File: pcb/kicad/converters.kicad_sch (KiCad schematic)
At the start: 48 parts, among them J2 NMJ4HCD2, U601 REF3033, U602 DAC7563SDGSR, U603 MCP6001-OT, U604 ADC141S626, U605 MCP6001-OT, U606 MCP6001-OT

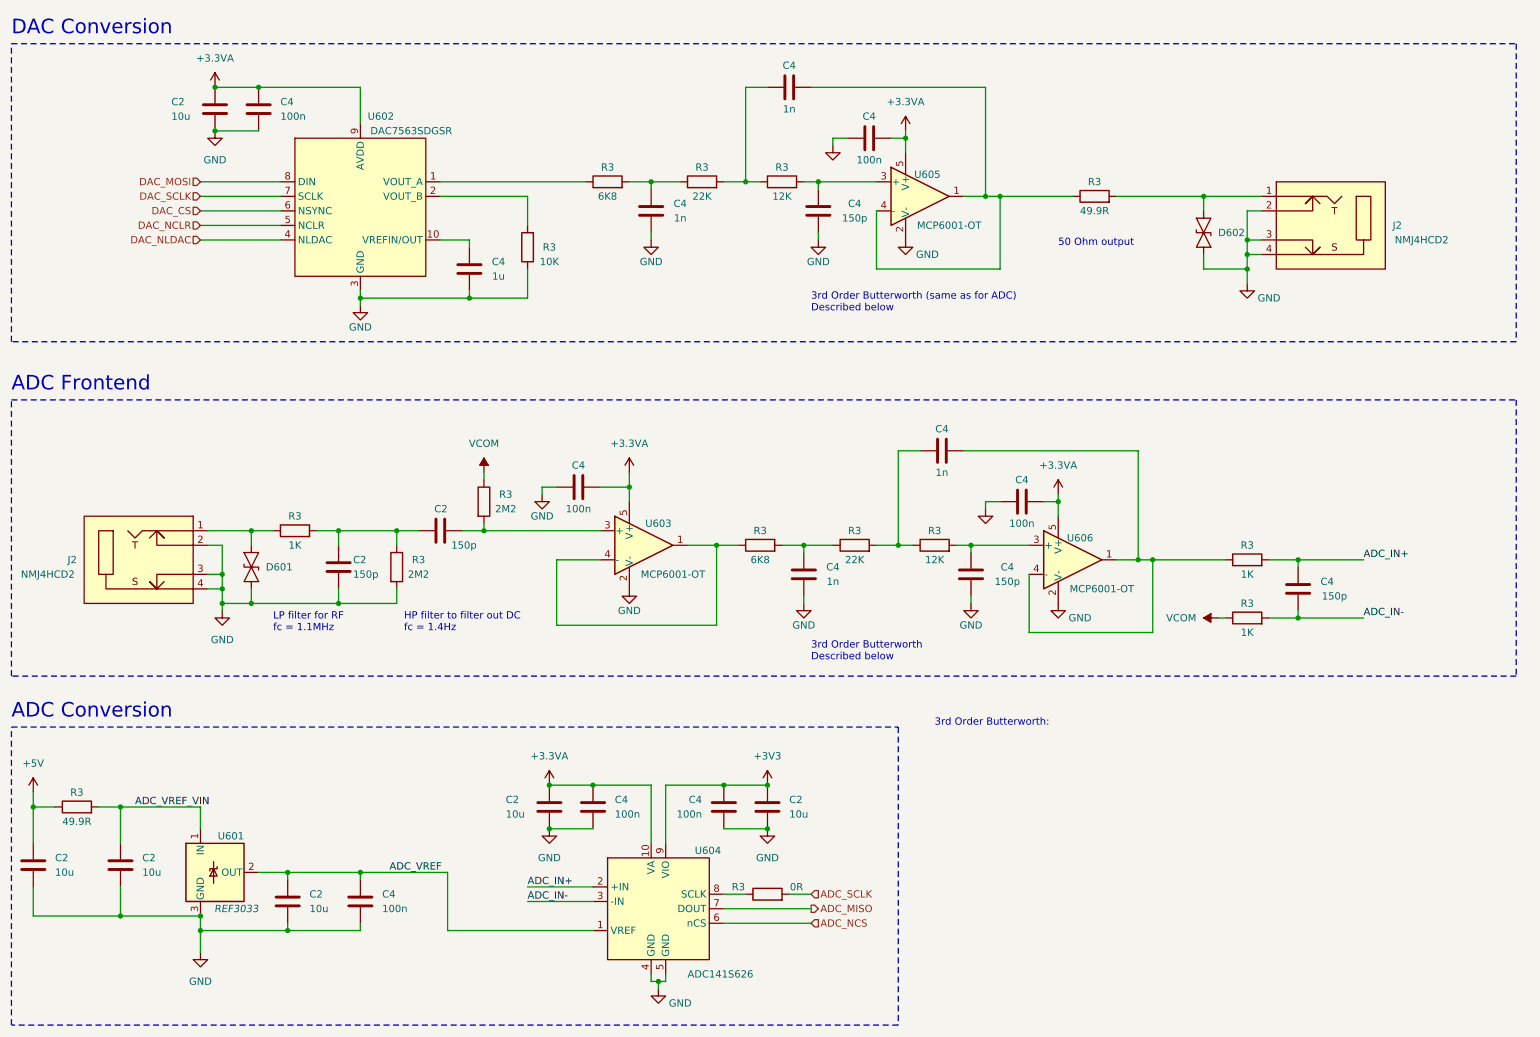
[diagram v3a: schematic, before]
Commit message: Add ltspice simulations.
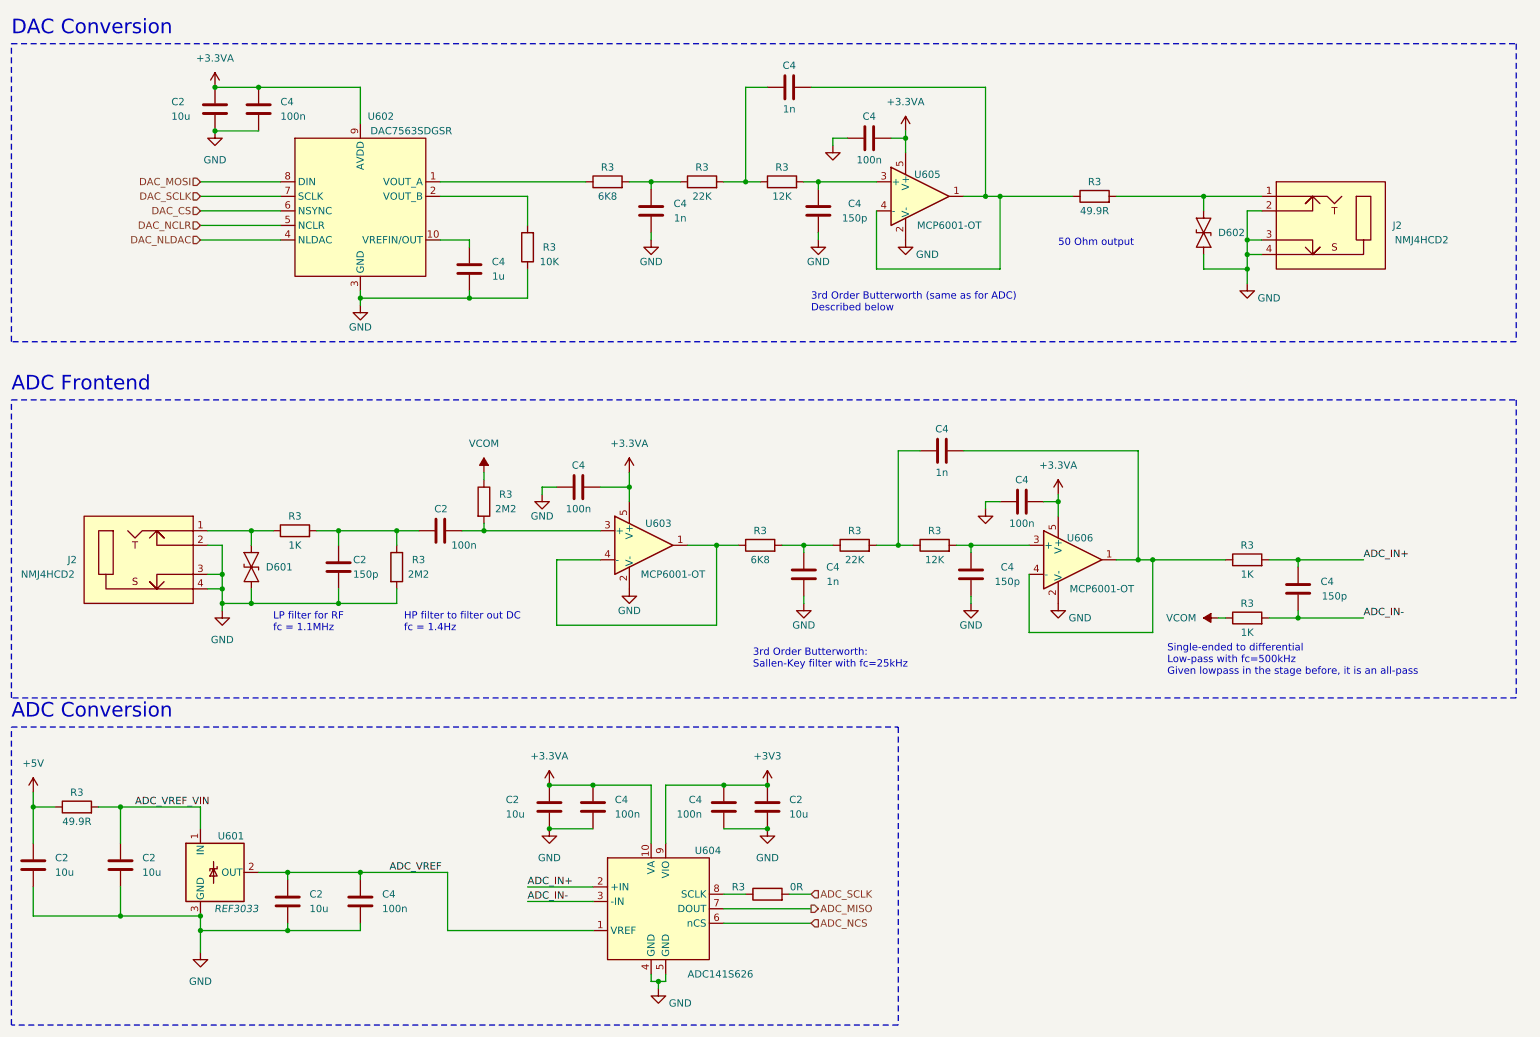
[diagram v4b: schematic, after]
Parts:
- C2: value 150p -> 100n
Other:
- note added: "3rd Order Butterworth: Sallen-Key filter with fc=25kHz"
- note added: "Single-ended to differential Low-pass with fc=500kHz Given lowpass in the stage before, it is an all-pass"
- note removed: "3rd Order Butterworth Described below"
- note removed: "3rd Order Butterworth:"
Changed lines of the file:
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@@
     (fill (type none))
   )
-  (rectangle (start 16.51 85.09) (end 279.4 133.35)
+  (rectangle (start 16.51 85.09) (end 279.4 137.16)
     (stroke (width 0) (type dash))
     (fill (type none))
@@
     (effects (font (size 2.54 2.54)) (justify left bottom))
   )
+  (text "3rd Order Butterworth:\nSallen-Key filter with fc=25kHz"
+    (at 146.05 132.08 0)
+    (effects (font (size 1.27 1.27)) (justify left bottom))
+  )
   (text "3rd Order Butterworth (same as for ADC)\nDescribed below"
     (at 156.21 69.85 0)
@@
     (effects (font (size 1.27 1.27)) (justify left bottom))
   )
-  (text "3rd Order Butterworth:" (at 177.8 142.24 0)
-    (effects (font (size 1.27 1.27)) (justify left bottom))
-  )
-  (text "3rd Order Butterworth\nDescribed below" (at 156.21 130.81 0)
+  (text "Single-ended to differential\nLow-pass with fc=500kHz\nGiven lowpass in the stage before, it is an all-pass"
+    (at 218.44 133.35 0)
     (effects (font (size 1.27 1.27)) (justify left bottom))
   )
@@
       (effects (font (size 1.27 1.27)) (justify left))
     )
-    (property "Value" "150p" (at 97.79 110.49 90)
-      (effects (font (size 1.27 1.27)) (justify left))
-    )
+    (property "Value" "100n" (at 97.79 110.49 90)
+      (effects (font (size 1.27 1.27)) (justify left))
+    )

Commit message: Add part numbers to components for ordering.
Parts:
- C2: Part Number (none) -> C0805C106M8RACTU
- C2, C4: Part Number (none) -> CC0805JRX7R9BB104
- C2, C4: Part Number (none) -> 885012207111
- C4: Part Number (none) -> C0805C102K2RAC
- C4: Part Number (none) -> CC0805KKX7R7BB105
- D601, D602: Part Number (none) -> PESD3V3L1BA,115
- J2: Part Number (none) -> NMJ4HCD2; Supplier Link (none) -> https://www.mouser.de/ProductDetail/Neutrik/NMJ4HCD2?qs=Szd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
- R3: Part Number (none) -> RP0805FRE0712KL
- R3: Part Number (none) -> CMP0805AFX-49R9ELF
- R3: Part Number (none) -> RT0805FRE071KL
- R3: Part Number (none) -> AC0805FR-0710K5L
- R3: Part Number (none) -> RT0805FRE1322KL
- R3: Part Number (none) -> CRCW08050000Z0EC
- R3: Part Number (none) -> RCV08052M20FKEA
- R3: Part Number (none) -> RT0805BRD076K8L
- U601: Part Number (none) -> REF3033AIDBZR; Supplier Link (none) -> https://www.digikey.de/en/products/detail/texas-instruments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
- U602: Part Number (none) -> DAC7563SDGSR; Supplier Link (none) -> https://www.digikey.de/en/products/detail/texas-instruments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
- U603, U605, U606: Part Number (none) -> MCP6001UT-I/OT; Supplier Link (none) -> https://www.digikey.de/en/products/detail/microchip-technol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
- U604: Part Number (none) -> ADC141S626; Supplier Link (none) -> https://www.digikey.de/en/products/detail/texas-instruments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
